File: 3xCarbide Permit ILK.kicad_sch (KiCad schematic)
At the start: 43 parts, among them J1 UT00104PH, J2 UT00104PH, J3 UT00104PH, J4 UT00104PH, J5 UT00104PH, J6 UT00104PH, SW1 2PB11, SW2 2PB11, SW3 2PB11, SW4 2PB11, SW5 2PB11, SW6 2PB11

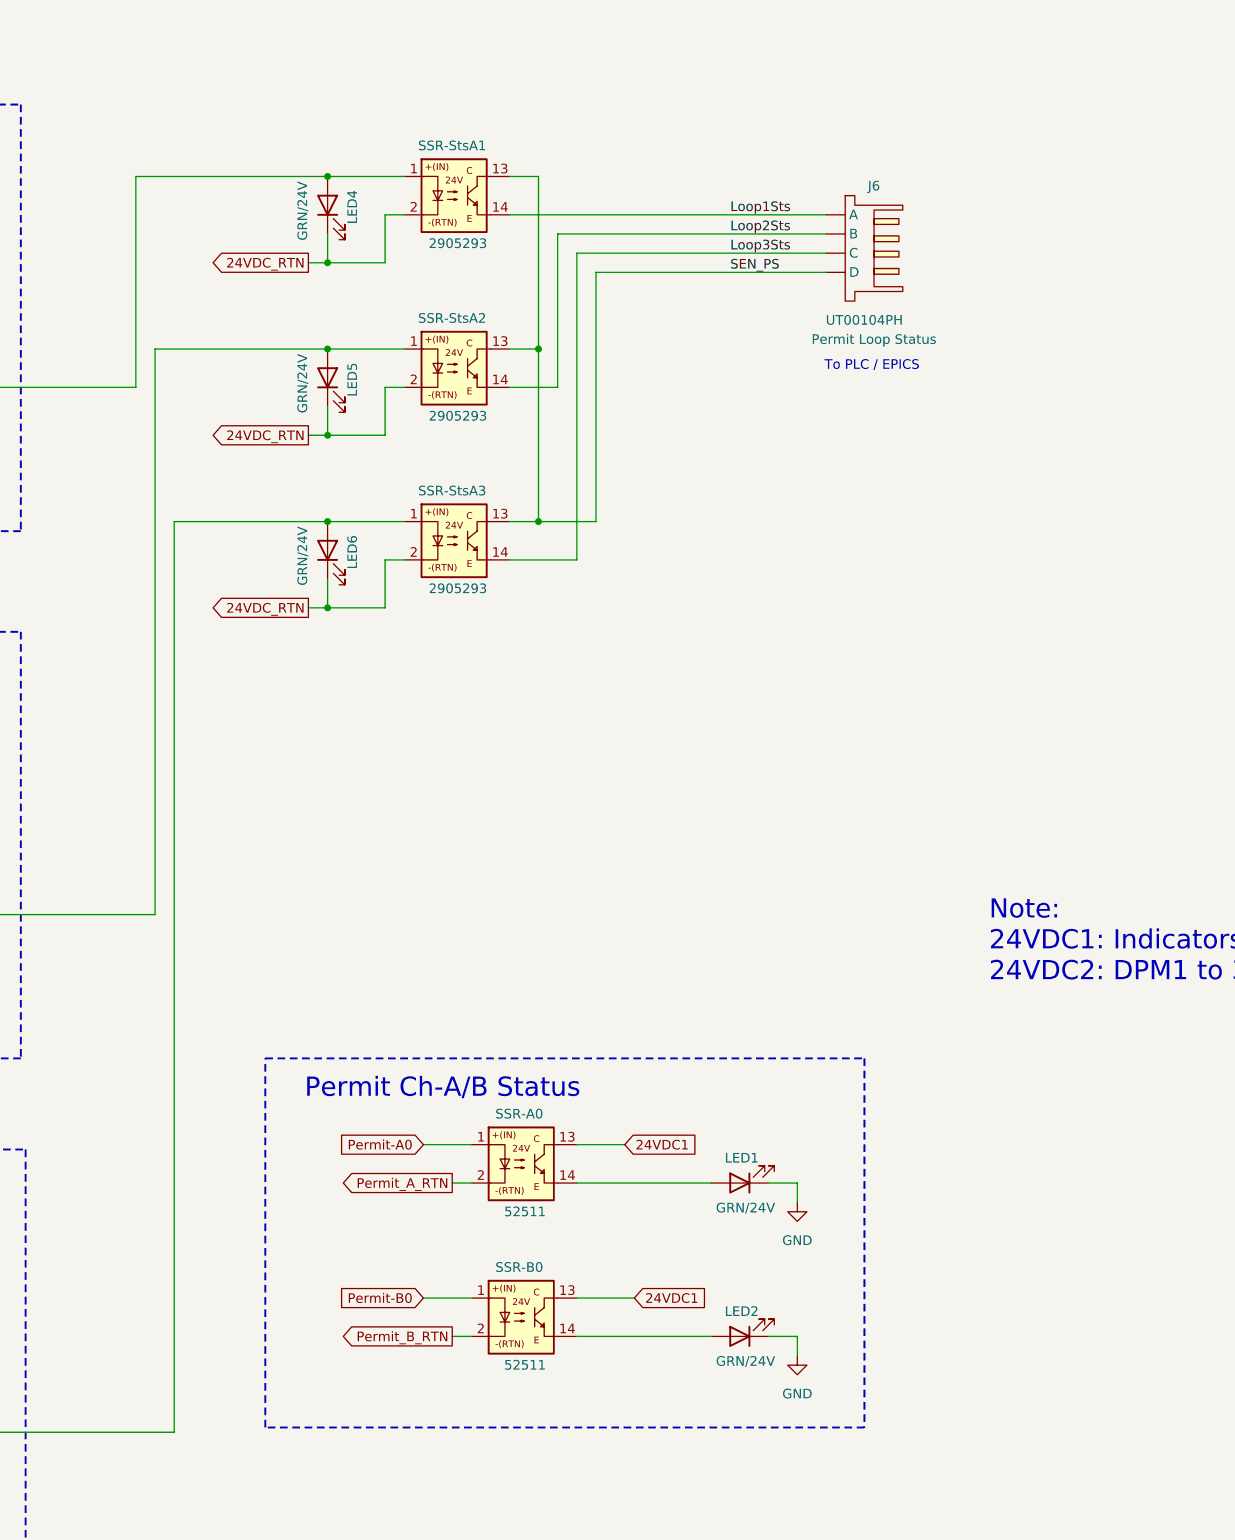
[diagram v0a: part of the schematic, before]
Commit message: Added Interface Cable and etc
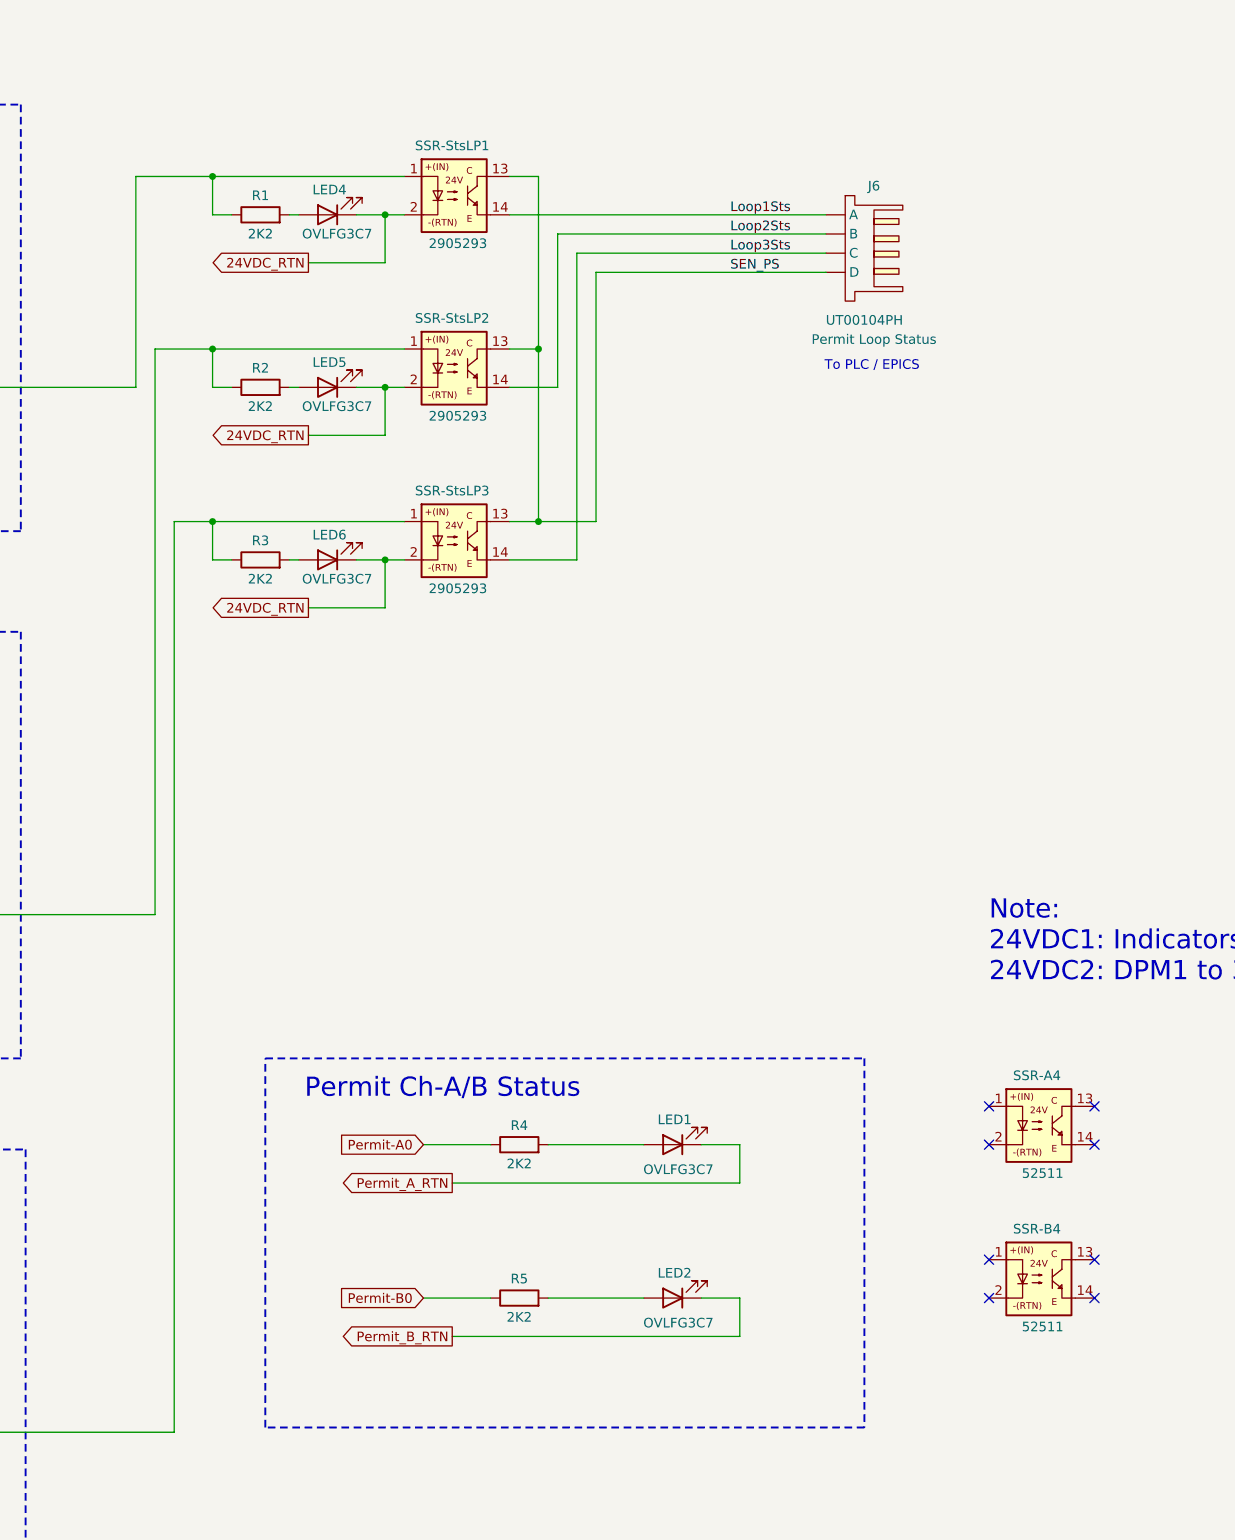
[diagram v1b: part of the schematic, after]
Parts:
- removed SSR-A0, SSR-B0: 52511, symbol JP_3xCarbide:SSR_MIRO_52511
- added R1, R2, R3, R4, R5: 2K2, symbol Device:R
- added SSR-A4, SSR-B4: 52511, symbol JP_3xCarbide:SSR_MIRO_52511
- LED1, LED2, LED4, LED5, LED6: value GRN/24V -> OVLFG3C7; Info (none) -> Green 525nm LED Indication - Discrete 3.4V Radial
- SSR-StsLP1: renamed from SSR-StsA1; Info (none) -> Loop Status
- SSR-StsLP2: renamed from SSR-StsA2; Info (none) -> Loop Status
- SSR-StsLP3: renamed from SSR-StsA3; Info (none) -> Loop Status
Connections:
- net Permit-A0: now also R4.1
- net Permit-B0: now also R5.1
- net Permit_A_RTN: now also LED1.1 (K)
- net Permit_B_RTN: now also LED2.1 (K)
- net at J2. (D): no longer TB-B1. (D)
- net at DPM1.1 (CN5): now also SSR-StsLP1.1, R1.1
- net at J1. (D): now also TB-A3. (D)
- net at LED2.2 (A): now also R5.2
- net at DPM3.1 (CN5): now also SSR-StsLP3.1, R3.1
- net at J4. (D): now also DPM2.4 (CN2)
- net at J5. (D): now also SSR-A3.13
- net at LED1.2 (A): now also R4.2
- removed net GND: LED1.1 (K), LED2.1 (K)
- new net: J2. (D), TB-B1. (D)
- new net: J1. (D), TB-A1. (D)
- new net: DPM2.1 (CN5), R2.1, SSR-StsLP2.1
- new net: LED4.2 (A), R1.2
- new net: LED5.2 (A), R2.2
- new net: J2. (D), TB-B3. (D)
- new net: LED6.2 (A), R3.2
- now unconnected: DPM2.1 (CN5), J2. (D)
- no-connect marks 36 -> 44
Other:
- moved on the sheet: LED1, LED2, LED4, LED5, LED6

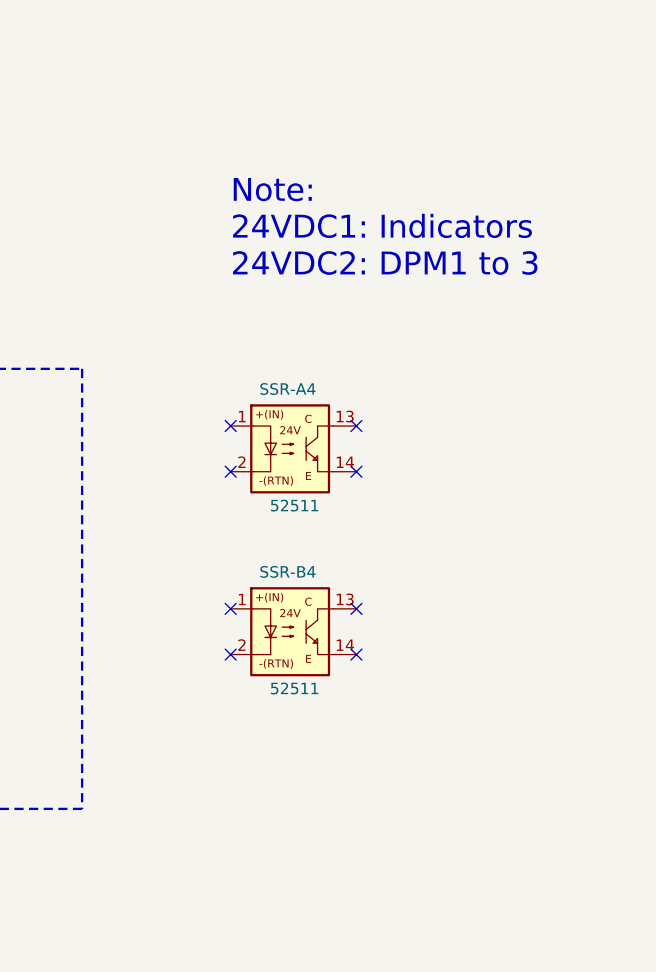
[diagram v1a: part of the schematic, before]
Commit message: Updated Interface cable
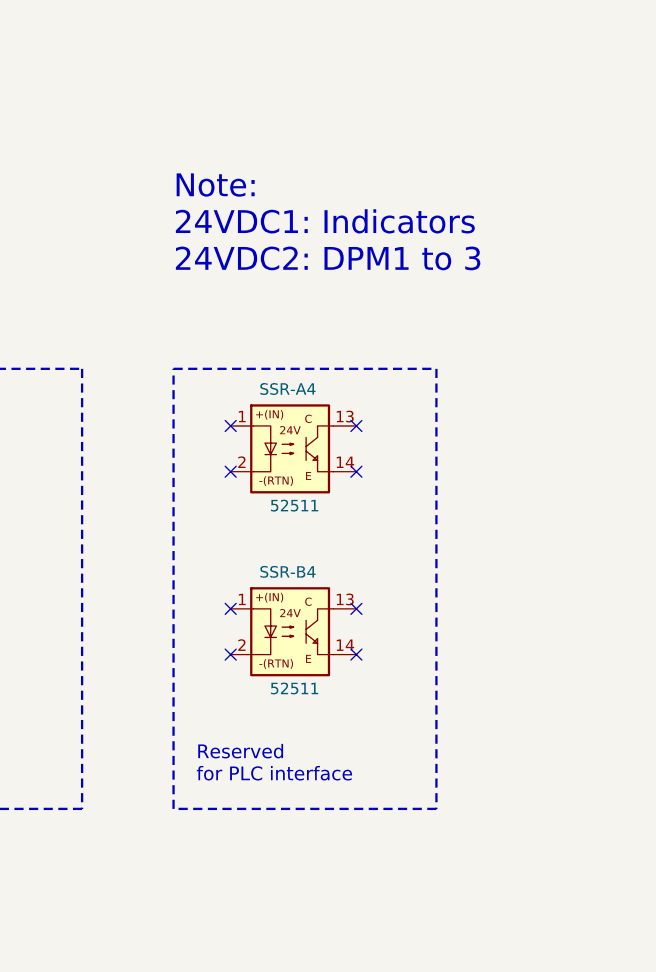
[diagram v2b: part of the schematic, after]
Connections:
- net at J2. (D): no longer TB-B1. (D)
- net at DPM1.1 (CN5): now also R1.1, SSR-StsLP1.1
- net at J1. (D): now also TB-A3. (D)
- net at DPM3.1 (CN5): now also R3.1, SSR-StsLP3.1
- net at J4. (D): now also DPM2.4 (CN2)
- net at J5. (D): now also SSR-A3.13
- new net: J2. (D), TB-B1. (D)
- new net: J1. (D), TB-A1. (D)
- new net: J2. (D), TB-B3. (D)
- now unconnected: J2. (D)
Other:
- note added: "Reserved for PLC interface"
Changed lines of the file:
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@@
+	)
+	(rectangle
+		(start 364.49 166.37)
+		(end 393.7 215.265)
+		(stroke
+			(width 0.254)
+			(type dash)
+			(color 132 132 132 1)
+		)
+		(fill
+			(type none)
+		)
 	)
 	(rectangle
@@
 		)
 	)
+	(text "Reserved \nfor PLC interface"
+		(exclude_from_sim no)
+		(at 367.03 208.28 0)
+		(effects
+			(font
+				(size 1.524 1.524)
+			)
+			(justify left top)
+		)
+	)
 	(text "Carbide Permit Current Loop 3 (Ch-A + Ch-B)"
 		(exclude_from_sim no)
@@
 	(text "Note:\n24VDC1: Indicators\n24VDC2: DPM1 to 3"
 		(exclude_from_sim no)
-		(at 370.84 145.288 0)
+		(at 364.49 144.78 0)
 		(effects
 			(font

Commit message: Clean up
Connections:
- net Permit-A0 is gone; now on net Permit-A: R4.1, TB-A2. (D)
- net Permit-B0 is gone; now on net Permit-B: R5.1, TB-B2. (D)
- net at J2. (D): no longer TB-B1. (D)
- net at DPM1.1 (CN5): now also R1.1, SSR-StsLP1.1
- net at J1. (D): now also TB-A3. (D)
- net Permit-B: now reaches TB-B2. (D)
- net at DPM3.1 (CN5): now also R3.1, SSR-StsLP3.1
- net at J4. (D): now also DPM2.4 (CN2)
- net at J5. (D): now also SSR-A3.13
- net Permit-A: now reaches TB-A2. (D)
- new net: J2. (D), TB-B1. (D)
- new net: J1. (D), TB-A1. (D)
- new net: J2. (D), TB-B3. (D)
- now unconnected: J2. (D)
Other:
- note added: "Note: 1) 24VDC1: Indicators 2) 24VDC2: DPM1 to 3 3) Indication LEDs (unless otherwise specified): GRN 4) Internal wiring: AWG #20 signal wire or equivalent"
- note removed: "Note: 24VDC1: Indicators 24VDC2: DPM1 to 3"
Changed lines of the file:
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@@
+		)
+	)
+	(text "Note:\n1) 24VDC1: Indicators\n2) 24VDC2: DPM1 to 3\n3) Indication LEDs (unless otherwise specified): GRN\n4) Internal wiring: AWG #20 signal wire or equivalent"
+		(exclude_from_sim no)
+		(at 274.32 116.84 0)
+		(effects
+			(font
+				(size 2.54 2.54)
+			)
+			(justify left top)
 		)
 	)
@@
 	(text "Reserved \nfor PLC interface"
 		(exclude_from_sim no)
-		(at 367.03 208.28 0)
+		(at 369.57 208.28 0)
 		(effects
 			(font
@@
 				(size 1.27 1.27)
 			)
-		)
-	)
-	(text "Note:\n24VDC1: Indicators\n24VDC2: DPM1 to 3"
-		(exclude_from_sim no)
-		(at 364.49 144.78 0)
-		(effects
-			(font
-				(size 2.54 2.54)
-			)
-			(justify left top)
 		)
 	)
@@
 		)
 	)
-	(global_label "Permit-B0"
+	(global_label "Permit-B"
 		(shape input)
 		(at 295.91 198.12 180)
@@
 		)
 		(property "Intersheetrefs" "${INTERSHEET_REFS}"
-			(at 282.7043 198.12 0)
+			(at 283.9138 198.12 0)
 			(hide yes)
 			(show_name no)
@@
 		)
 	)
-	(global_label "Permit-B0"
+	(global_label "Permit-B"
 		(shape input)
 		(at 78.74 166.37 0)
@@
 		)
 		(property "Intersheetrefs" "${INTERSHEET_REFS}"
-			(at 91.9457 166.37 0)
+			(at 90.7362 166.37 0)
 			(hide yes)
 			(show_name no)
@@
 		)
 	)
-	(global_label "Permit-A0"
+	(global_label "Permit-A"
 		(shape output)
 		(at 78.74 69.85 0)
@@
 		)
 		(property "Intersheetrefs" "${INTERSHEET_REFS}"
-			(at 91.7643 69.85 0)
+			(at 90.5548 69.85 0)
 			(hide yes)
 			(show_name no)
@@
 		)
 	)
-	(global_label "Permit-A0"
+	(global_label "Permit-A"
 		(shape input)
 		(at 295.91 177.8 180)
@@
 		)
 		(property "Intersheetrefs" "${INTERSHEET_REFS}"
-			(at 282.8857 177.8 0)
-			(hide yes)
-			(show_name no)
+			(at 284.0952 177.8 0)
+			(hide yes)
+			(show_name no)

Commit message: Updated PS and clean up
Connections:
- net 24VDC1 is gone; now on net 24VDC: DPM1.2 (CN5), DPM2.2 (CN5), DPM3.2 (CN5)
- net 24VDC2 is gone; now on net 24VDC: DPM1.2(+) (CN1), DPM2.2(+) (CN1), DPM3.2(+) (CN1)
- net at J2. (D): no longer TB-B1. (D)
- net at DPM1.1 (CN5): now also R1.1, SSR-StsLP1.1
- net 24VDC: now reaches DPM1.2 (CN5)
- net at J1. (D): now also TB-A3. (D)
- net at DPM3.1 (CN5): now also R3.1, SSR-StsLP3.1
- net at J4. (D): now also DPM2.4 (CN2)
- net at J5. (D): now also SSR-A3.13
- new net: J2. (D), TB-B1. (D)
- new net: J1. (D), TB-A1. (D)
- new net: J2. (D), TB-B3. (D)
- now unconnected: J2. (D)
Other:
- note added: "Note: 1) 24VDC: Indicators & DPM1 to 3 2) Indication LEDs (unless otherwise specified): GRN 3) Internal wiring: AWG #20 signal wire or equivalent"
- note added: "Permit Current Loop (1 to 3): Supply XS13-21 (J#.C) (+5 V / 40 mA max.) → Dry Contactor (A/B) → Return = XS13-9 (J#.D) → Carbide Internal Optocoupler (Laser Permit)"
- note removed: "Note: 1) 24VDC1: Indicators 2) 24VDC2: DPM1 to 3 3) Indication LEDs (unless otherwise specified): GRN 4) Internal wiring: AWG #20 signal wire or equivalent"
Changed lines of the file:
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@@
 		(title "LCLS-II BCS CARBIDE PERMIT INTERLOCK")
 		(date "2026-08-21")
-		(rev "1.01")
+		(rev "1.02")
 		(company "SLAC")
 		(comment 1 "ENGR: J.Park")
@@
 		)
 	)
-	(text "Note:\n1) 24VDC1: Indicators\n2) 24VDC2: DPM1 to 3\n3) Indication LEDs (unless otherwise specified): GRN\n4) Internal wiring: AWG #20 signal wire or equivalent"
+	(text "Note:\n1) 24VDC: Indicators & DPM1 to 3\n2) Indication LEDs (unless otherwise specified): GRN\n3) Internal wiring: AWG #20 signal wire or equivalent"
 		(exclude_from_sim no)
 		(at 274.32 116.84 0)
@@
 			(font
 				(size 2.54 2.54)
+			)
+			(justify left top)
+		)
+	)
+	(text "Permit Current Loop (1 to 3): \nSupply XS13-21 (J#.C) (+5 V / 40 mA max.) \n  → Dry Contactor (A/B) → Return = XS13-9 (J#.D)\n  → Carbide Internal Optocoupler (Laser Permit) "
+		(exclude_from_sim no)
+		(at 198.12 238.76 0)
+		(effects
+			(font
+				(size 1.27 1.27)
 			)
 			(justify left top)
@@
 		)
 	)
-	(global_label "24VDC1"
+	(global_label "24VDC"
 		(shape input)
 		(at 218.44 80.01 0)
@@
 		)
 		(property "Intersheetrefs" "${INTERSHEET_REFS}"
-			(at 228.6823 80.01 0)
+			(at 227.4728 80.01 0)
 			(hide yes)
 			(show_name no)
@@
 		)
 	)
-	(global_label "24VDC1"
+	(global_label "24VDC"
 		(shape input)
 		(at 220.98 218.44 0)
@@
 		)
 		(property "Intersheetrefs" "${INTERSHEET_REFS}"
-			(at 231.2223 218.44 0)
+			(at 230.0128 218.44 0)
 			(hide yes)
 			(show_name no)
@@
 		)
 	)
-	(global_label "24VDC1"
+	(global_label "24VDC"
 		(shape input)
 		(at 219.71 149.86 0)
@@
 		)
 		(property "Intersheetrefs" "${INTERSHEET_REFS}"
-			(at 229.9523 149.86 0)
+			(at 228.7428 149.86 0)
 			(hide yes)
 			(show_name no)
@@
 		)
 	)
-	(global_label "24VDC2"
+	(global_label "24VDC"
 		(shape input)
 		(at 177.8 86.36 180)
@@
 		)
 		(property "Intersheetrefs" "${INTERSHEET_REFS}"
-			(at 167.5577 86.36 0)
+			(at 168.7672 86.36 0)
 			(hide yes)
 			(show_name no)
@@
 		)
 	)
-	(global_label "24VDC2"
+	(global_label "24VDC"
 		(shape input)
 		(at 180.34 224.79 180)
@@
 		)
 		(property "Intersheetrefs" "${INTERSHEET_REFS}"
-			(at 170.0977 224.79 0)
+			(at 171.3072 224.79 0)
 			(hide yes)
 			(show_name no)
@@
 		)
 	)
-	(global_label "24VDC2"
+	(global_label "24VDC"
 		(shape input)
 		(at 179.07 156.21 180)
@@
 		)
 		(property "Intersheetrefs" "${INTERSHEET_REFS}"
-			(at 168.8277 156.21 0)
-			(hide yes)
-			(show_name no)
+			(at 170.0372 156.21 0)
+			(hide yes)
+			(show_name no)
